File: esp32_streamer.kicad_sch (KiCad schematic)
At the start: 35 parts, among them J1 105017-1001, J2 SJ1-3533NS, U1 PCM5122PW, U2 ESP32-WROVER-EM213EH2864PH3Q0, U3 NCP167BMX330TBG, U4 NCP167BMX330TBG

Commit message: added a few backups
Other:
- note added: "TODO Audio grade caps for analog RC circuit? Rx Tx header for programming Power LED Bigger LDO? The one on this is tiny. Maybe Rx Tx leds USB-C for power ESD - use TVS diode"
- note removed: "TODO Audio grade caps for analog RC circuit? Rx Tx header for programming Power LED Maybe Rx Tx leds USB socket - check schematic ESD - use MOSFET rather than Shottky diode"
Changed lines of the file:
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@@
     (stroke (width 0) (type default) (color 0 0 0 0))
   )
-  (text "TODO\nAudio grade caps for analog RC circuit?\nRx Tx header for programming\nPower LED\nMaybe Rx Tx leds\nUSB socket - check schematic\nESD - use MOSFET rather than Shottky diode"
+  (text "TODO\nAudio grade caps for analog RC circuit?\nRx Tx header for programming\nPower LED\nBigger LDO? The one on this is tiny.\nMaybe Rx Tx leds\nUSB-C for power\nESD - use TVS diode"
     (at 19.05 190.5 0)
     (effects (font (size 1.27 1.27)) (justify left bottom))

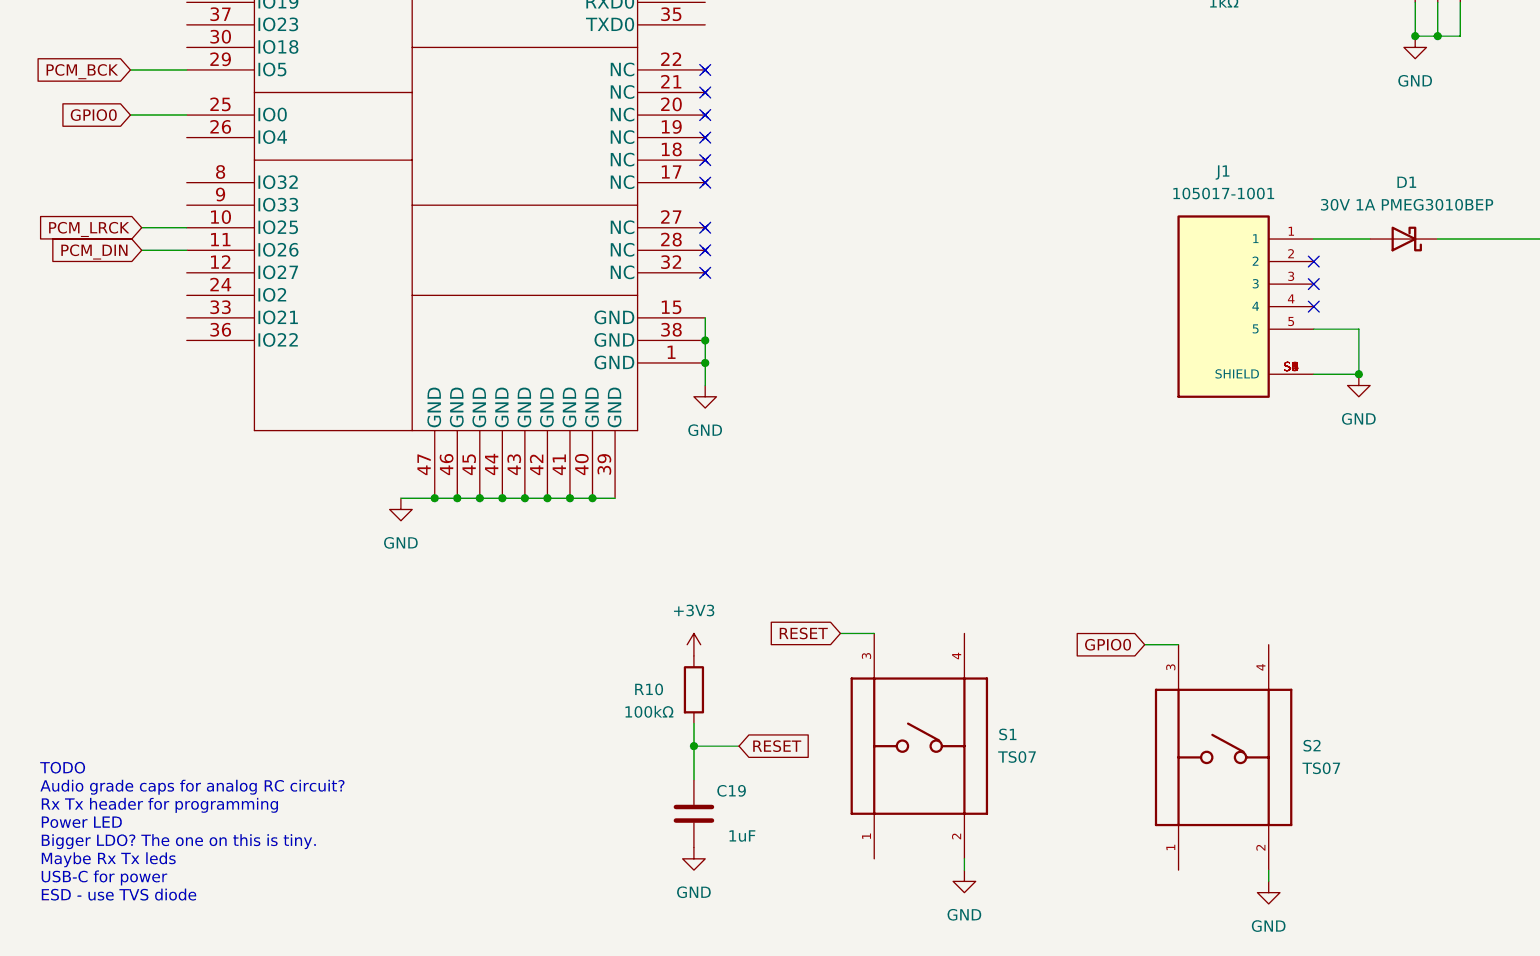
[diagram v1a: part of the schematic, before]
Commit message: removed backups and started changes on USB recepticle
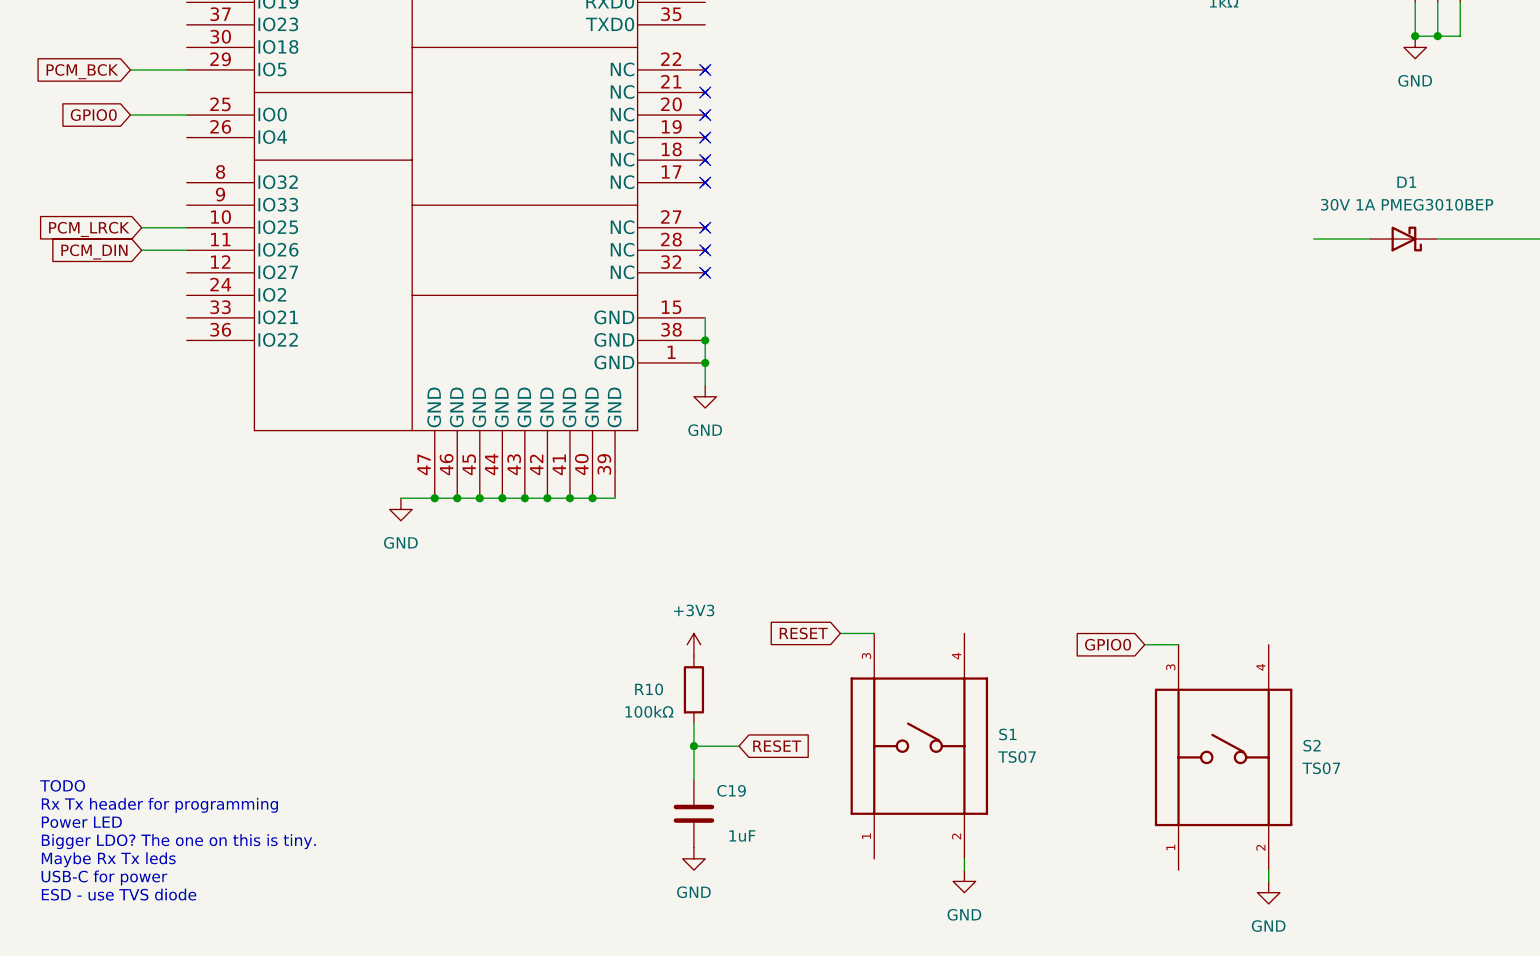
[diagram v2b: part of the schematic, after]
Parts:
- removed J1: 105017-1001, Connector_USB:USB_Micro-AB_Molex_47590-0001, symbol 105017-1001:105017-1001
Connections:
- no-connect marks 13 -> 10
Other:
- note added: "TODO Rx Tx header for programming Power LED Bigger LDO? The one on this is tiny. Maybe Rx Tx leds USB-C for power ESD - use TVS diode"
- note removed: "TODO Audio grade caps for analog RC circuit? Rx Tx header for programming Power LED Bigger LDO? The one on this is tiny. Maybe Rx Tx leds USB-C for power ESD - use TVS diode"
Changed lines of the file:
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@@
   (junction (at 41.91 25.4) (diameter 0) (color 0 0 0 0)
-  )
-  (junction (at 167.64 130.81) (diameter 0) (color 0 0 0 0)
   )
   (junction (at 204.47 115.57) (diameter 0) (color 0 0 0 0)
@@
   (no_connect (at 93.98 99.06))
   (no_connect (at 93.98 96.52))
-  (no_connect (at 162.56 120.65))
-  (no_connect (at 162.56 118.11))
-  (no_connect (at 162.56 123.19))
   (wire (pts (xy 41.91 25.4) (xy 41.91 30.48))
     (stroke (width 0) (type default) (color 0 0 0 0))
@@
     (stroke (width 0) (type default) (color 0 0 0 0))
   )
-  (wire (pts (xy 167.64 125.73) (xy 167.64 130.81))
-    (stroke (width 0) (type default) (color 0 0 0 0))
-  )
   (wire (pts (xy 30.48 114.3) (xy 35.56 114.3))
     (stroke (width 0) (type default) (color 0 0 0 0))
@@
     (stroke (width 0) (type default) (color 0 0 0 0))
   )
-  (wire (pts (xy 162.56 130.81) (xy 167.64 130.81))
-    (stroke (width 0) (type default) (color 0 0 0 0))
-  )
   (wire (pts (xy 67.31 41.91) (xy 80.01 41.91))
     (stroke (width 0) (type default) (color 0 0 0 0))
@@
     (stroke (width 0) (type default) (color 0 0 0 0))
   )
-  (wire (pts (xy 162.56 125.73) (xy 167.64 125.73))
-    (stroke (width 0) (type default) (color 0 0 0 0))
-  )
   (wire (pts (xy 214.63 50.8) (xy 214.63 52.07))
     (stroke (width 0) (type default) (color 0 0 0 0))
@@
     (stroke (width 0) (type default) (color 0 0 0 0))
   )
-  (text "TODO\nAudio grade caps for analog RC circuit?\nRx Tx header for programming\nPower LED\nBigger LDO? The one on this is tiny.\nMaybe Rx Tx leds\nUSB-C for power\nESD - use TVS diode"
+  (text "TODO\nRx Tx header for programming\nPower LED\nBigger LDO? The one on this is tiny.\nMaybe Rx Tx leds\nUSB-C for power\nESD - use TVS diode"
     (at 19.05 190.5 0)
     (effects (font (size 1.27 1.27)) (justify left bottom))
@@
     )
     (property "Datasheet" "" (id 3) (at 228.6 35.56 0)
-      (effects (font (size 1.27 1.27)) hide)
-    )
-    (pin "1")
-  )
-  (symbol (lib_id "power:GND") (at 167.64 130.81 0) (unit 1)
-    (in_bom yes) (on_board yes) (fields_autoplaced)
-    (property "Reference" "#PWR?" (id 0) (at 167.64 137.16 0)
-      (effects (font (size 1.27 1.27)) hide)
-    )
-    (property "Value" "GND" (id 1) (at 167.64 135.89 0))
-    (property "Footprint" "" (id 2) (at 167.64 130.81 0)
-      (effects (font (size 1.27 1.27)) hide)
-    )
-    (property "Datasheet" "" (id 3) (at 167.64 130.81 0)
       (effects (font (size 1.27 1.27)) hide)
     )
@@
     (pin "1")
     (pin "2")
-  )
-  (symbol (lib_id "105017-1001:105017-1001") (at 152.4 123.19 0) (unit 1)
-    (in_bom yes) (on_board yes) (fields_autoplaced)
-    (property "Reference" "J1" (id 0) (at 152.4 107.95 0))
-    (property "Value" "105017-1001" (id 1) (at 152.4 110.49 0))
-    (property "Footprint" "Connector_USB:USB_Micro-AB_Molex_47590-0001" (id 2) (at 152.4 123.19 0)
-      (effects (font (size 1.27 1.27)) (justify left bottom) hide)
-    )
-    (property "Datasheet" "" (id 3) (at 152.4 123.19 0)
-      (effects (font (size 1.27 1.27)) (justify left bottom) hide)
-    )
-    (property "STANDARD" "Manufacturer Recommendations" (id 4) (at 152.4 123.19 0)
-      (effects (font (size 1.27 1.27)) (justify left bottom) hide)
-    )
-    (property "PARTREV" "F" (id 5) (at 152.4 123.19 0)
-      (effects (font (size 1.27 1.27)) (justify left bottom) hide)
-    )
-    (property "MAXIMUM_PACKAGE_HIEGHT" "2.9mm" (id 6) (at 152.4 123.19 0)
-      (effects (font (size 1.27 1.27)) (justify left bottom) hide)
-    )
-    (property "MANUFACTURER" "MOLEX" (id 7) (at 152.4 123.19 0)
-      (effects (font (size 1.27 1.27)) (justify left bottom) hide)
-    )
-    (pin "1")
-    (pin "2")
-    (pin "3")
-    (pin "4")
-    (pin "5")
-    (pin "S1")
-    (pin "S2")
-    (pin "S3")
-    (pin "S4")
-    (pin "S5")
-    (pin "S6")
   )
   (symbol (lib_id "project:SJ1-3533NS") (at 259.08 45.72 180) (unit 1)
@@
       (reference "#PWR?") (unit 1) (value "GND") (footprint "")
     )
-    (path "/0707b0b0-161a-466b-9606-46760ba72f28"
-      (reference "#PWR?") (unit 1) (value "GND") (footprint "")
-    )
     (path "/1b4410e8-0eb1-4e2f-b46b-e668e1a29827"
       (reference "#PWR?") (unit 1) (value "+3.3VA") (footprint "")
@@
       (reference "D1") (unit 1) (value "30V 1A PMEG3010BEP") (footprint "Diode_SMD:D_SOD-128")
     )
-    (path "/97af06ae-9ce6-4e9e-851c-62508e96d9e3"
-      (reference "J1") (unit 1) (value "105017-1001") (footprint "Connector_USB:USB_Micro-AB_Molex_47590-0001")
-    )
     (path "/9ee66366-9074-4bc0-8447-8c0b7199acdf"

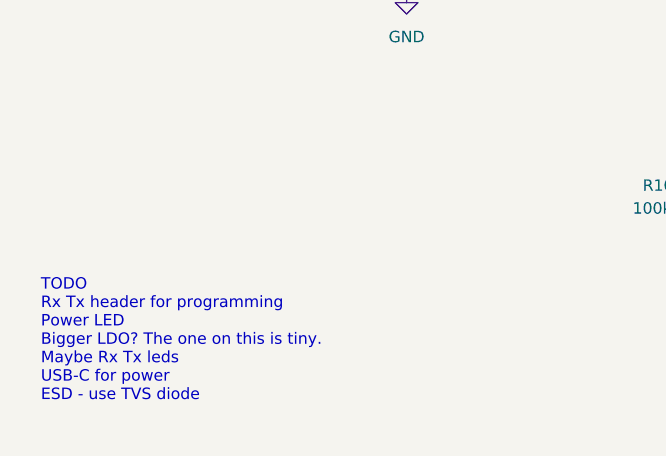
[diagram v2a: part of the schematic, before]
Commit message: minor update on text label TODO
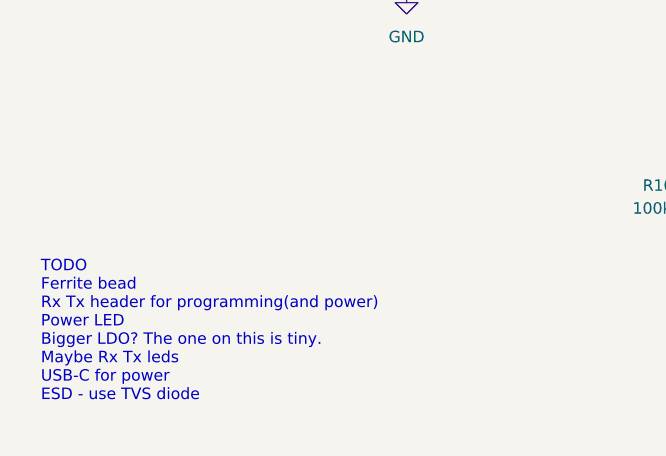
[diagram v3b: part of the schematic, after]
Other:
- note added: "TODO Ferrite bead Rx Tx header for programming(and power) Power LED Bigger LDO? The one on this is tiny. Maybe Rx Tx leds USB-C for power ESD - use TVS diode"
- note removed: "TODO Rx Tx header for programming Power LED Bigger LDO? The one on this is tiny. Maybe Rx Tx leds USB-C for power ESD - use TVS diode"
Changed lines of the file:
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@@
     (stroke (width 0) (type default) (color 0 0 0 0))
   )
-  (text "TODO\nRx Tx header for programming\nPower LED\nBigger LDO? The one on this is tiny.\nMaybe Rx Tx leds\nUSB-C for power\nESD - use TVS diode"
+  (text "TODO\nFerrite bead\nRx Tx header for programming(and power)\nPower LED\nBigger LDO? The one on this is tiny.\nMaybe Rx Tx leds\nUSB-C for power\nESD - use TVS diode"
     (at 19.05 190.5 0)
     (effects (font (size 1.27 1.27)) (justify left bottom))

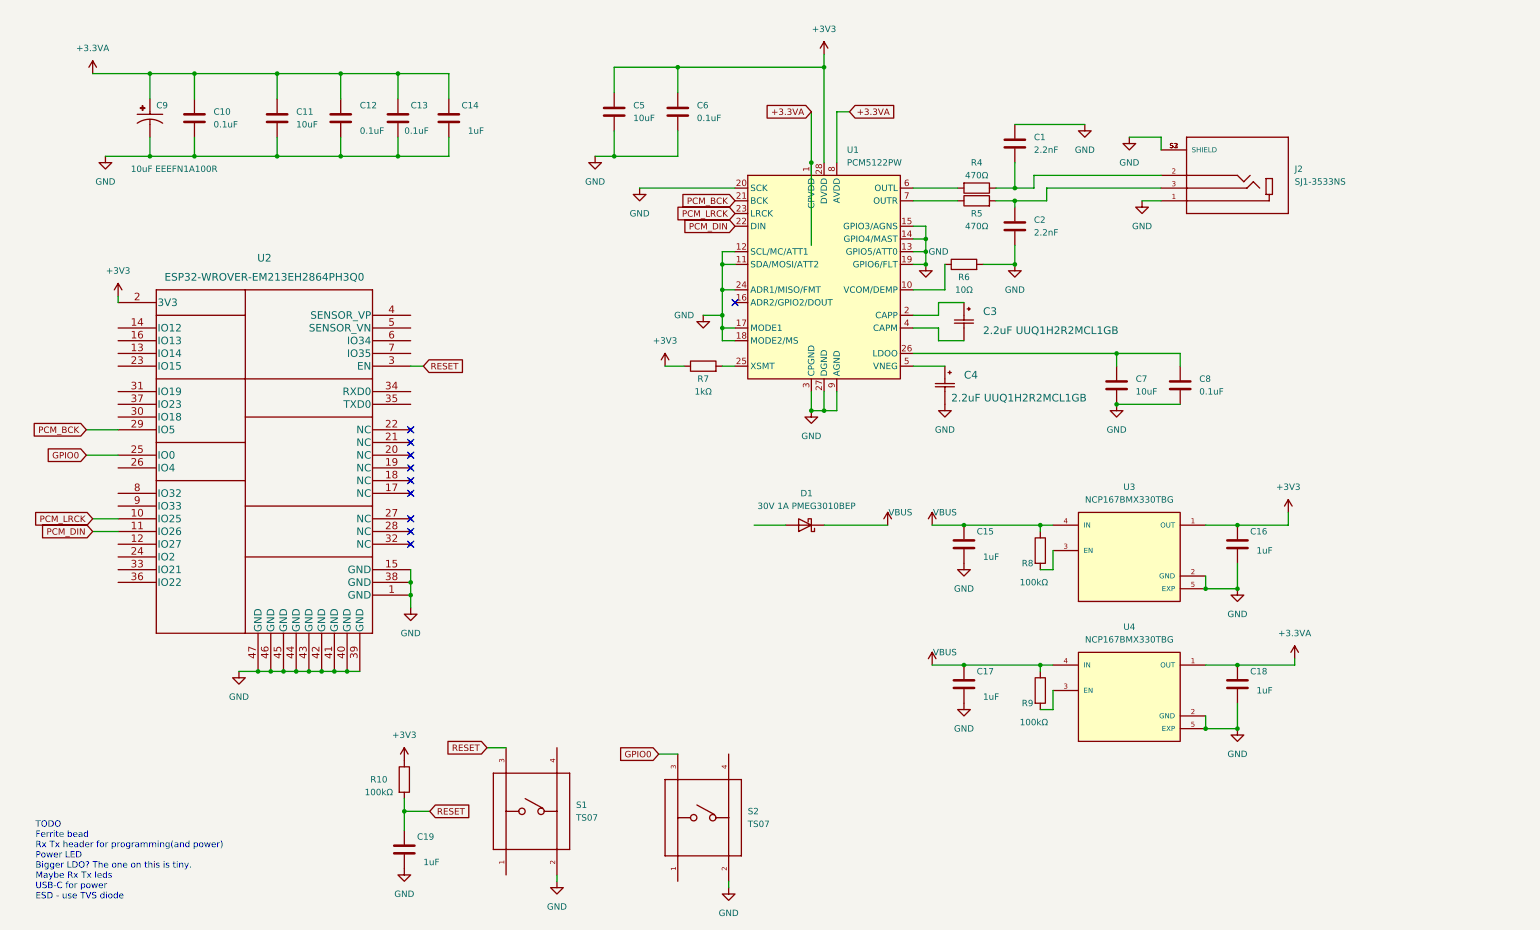
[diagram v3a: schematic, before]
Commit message: Added new LDO, USB connector and ESD protection on USB power line
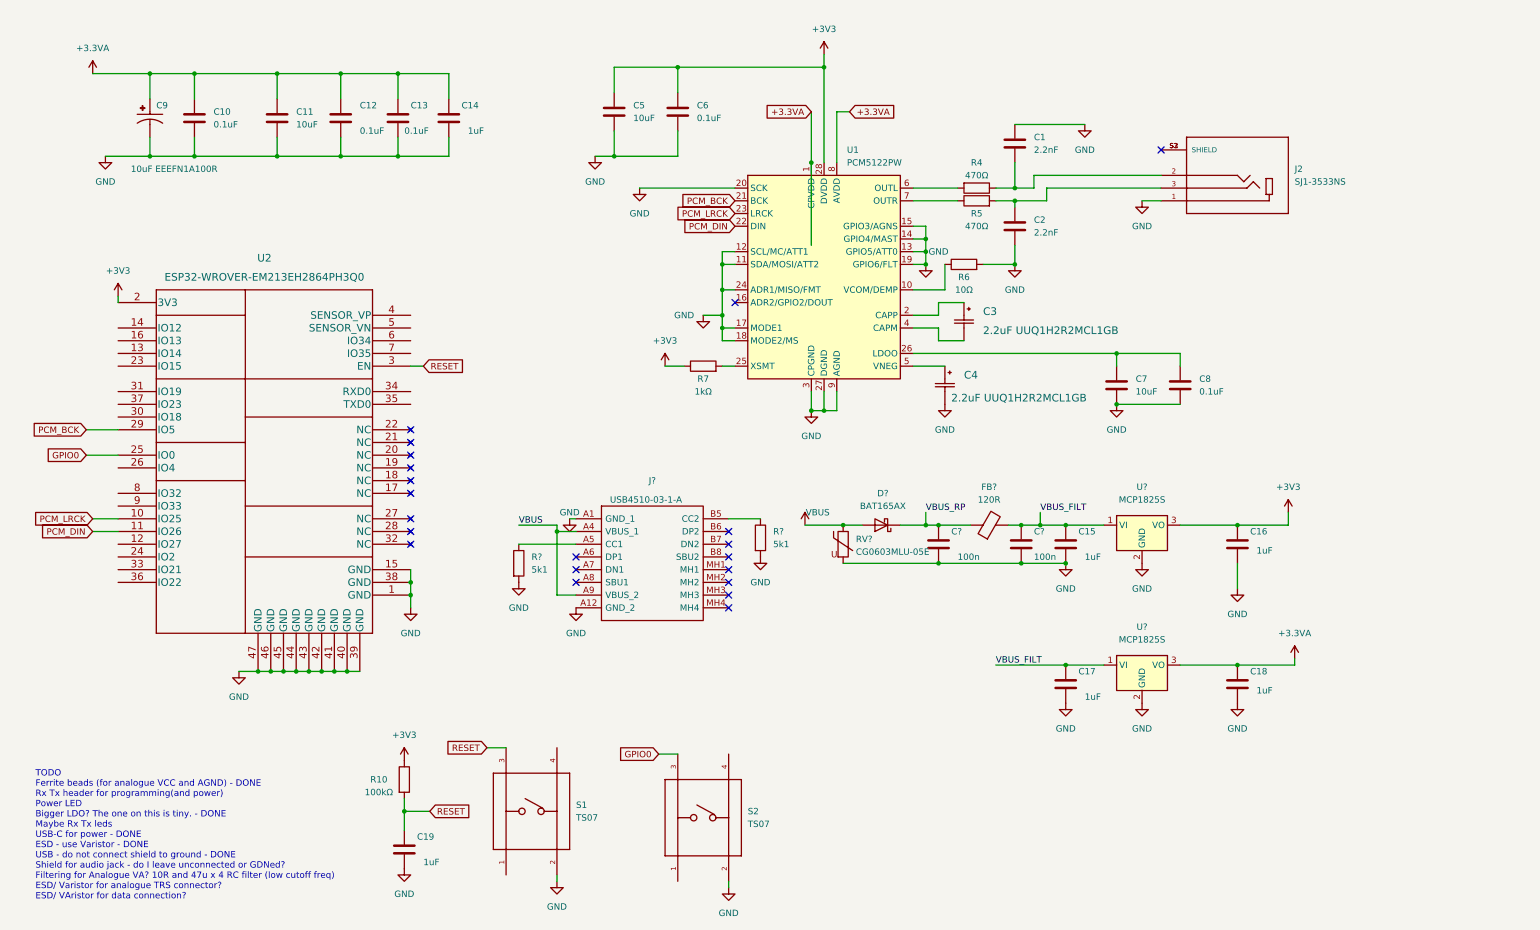
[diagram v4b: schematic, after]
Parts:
- removed D1: 30V 1A PMEG3010BEP, Diode_SMD:D_SOD-128, symbol Device:D_Schottky
- removed R8, R9: 100kΩ, Resistor_SMD:R_0603_1608Metric, symbol Device:R
- removed U3, U4: NCP167BMX330TBG, REG_NCP167BMX330TBG, symbol NCP167BMX330TBG:NCP167BMX330TBG
- added C? (x2): 100n, Capacitor_SMD:C_0805_2012Metric, symbol Device:C
- added D?: BAT165AX, Diode_SMD:D_SOD-323, symbol Device:D_Schottky
- added FB?: 120R, Resistor_SMD:R_0603_1608Metric, symbol Device:FerriteBead
- added J?: USB4510-03-1-A, library:USB4510031A, symbol USB4510-03-1-A:USB4510-03-1-A
- added R? (x2): 5k1, symbol Device:R
- added RV?: CG0603MLU-05E, Resistor_SMD:R_0603_1608Metric, symbol Device:Varistor
- added U? (x2): MCP1825S, Package_TO_SOT_SMD:SOT-223-3_TabPin2, symbol Regulator_Linear:MCP1825S
- J2: footprint CUI_SJ1-3533NS -> library:CUI_SJ1-3533NS
- S1, S2: footprint SW_TS07-667-37-BK-260-SMT-TR -> library:SW_TS07-667-37-BK-260-SMT-TR
- U2: footprint IC38_ESP32-WROVER-EM213EH2864PH3Q0_EXP -> library:ESP32-WROVER-EM213EH2864PH3Q0
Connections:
- net +3.3VA: now also U?.3 (VO)
- net +3V3: now also U?.3 (VO)
- net GND: now also C?.2, C?.2, J?.A1 (GND_1), J?.A12 (GND_2), R?.2, R?.2, RV?.2, U?.2 (GND), U?.2 (GND); no longer J2.S1 (SHIELD), J2.S2 (SHIELD), J2.S3 (SHIELD)
- net VBUS: now also D?.2 (A), J?.A4 (VBUS_1), J?.A9 (VBUS_2), RV?.1; no longer C15.1, C17.1
- new net: J?.A5 (CC1), R?.1
- new net: J2.S1 (SHIELD), J2.S2 (SHIELD), J2.S3 (SHIELD)
- new net: J?.B5 (CC2), R?.1
- new net VBUS_FILT: C15.1, C17.1, C?.1, FB?.2, U?.1 (VI), U?.1 (VI)
- new net VBUS_RP: C?.1, D?.1 (K), FB?.1
- no-connect marks 10 -> 21
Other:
- note added: "TODO Ferrite beads (for analogue VCC and AGND) - DONE Rx Tx header for programming(and power) Power LED Bigger LDO? The one on this is tiny. - DONE Maybe Rx Tx leds USB-C for power - DONE ESD - use Varistor - DONE USB - do not connect shield to ground - DONE Shield for audio jack - do I leave unconnected or GDNed? Filtering for Analogue VA? 10R and 47u x 4 RC filter (low cutoff freq) ESD/ Varisto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"
- note removed: "TODO Ferrite bead Rx Tx header for programming(and power) Power LED Bigger LDO? The one on this is tiny. Maybe Rx Tx leds USB-C for power ESD - use TVS diode"
- moved on the sheet: C15, C17
